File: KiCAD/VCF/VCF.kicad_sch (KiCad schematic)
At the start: 49 parts, among them J1 FM, J2 CV, J3 IN, J4 OUT, J5 Conn_01x03, J6 Conn_01x03, Q1 2N3904, SW1 SW_SPDT, SW2 SW_SPDT, U1 TL072, U2 TL072, U3 UA776, U4 UA776, U5 TL072

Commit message: Vertical Resistor Footprint
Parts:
- R1, R10, R11, R12, R13, R14, R15, R16, R17, R18, R19, R2, R20, R21, R22, R23, R24, R25, R26, R27, R3, R4, R5, R6, R7, R8, R9: footprint HackSynth:R_Axial_DIN0207_L6.3mm_D2.5mm_P7.62mm_Horizontal -> HackSynth:R_Vertical_P2.54mm
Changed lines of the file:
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@@
 			)
 		)
-		(property "Footprint" "HackSynth:R_Axial_DIN0207_L6.3mm_D2.5mm_P7.62mm_Horizontal"
+		(property "Footprint" "HackSynth:R_Vertical_P2.54mm"
 			(at 116.84 170.942 90)
 			(effects
@@
 			)
 		)
-		(property "Footprint" "HackSynth:R_Axial_DIN0207_L6.3mm_D2.5mm_P7.62mm_Horizontal"
+		(property "Footprint" "HackSynth:R_Vertical_P2.54mm"
 			(at 92.71 117.602 90)
 			(effects
@@
 			)
 		)
-		(property "Footprint" "HackSynth:R_Axial_DIN0207_L6.3mm_D2.5mm_P7.62mm_Horizontal"
+		(property "Footprint" "HackSynth:R_Vertical_P2.54mm"
 			(at 101.6 78.232 90)
 			(effects
@@
 			)
 		)
-		(property "Footprint" "HackSynth:R_Axial_DIN0207_L6.3mm_D2.5mm_P7.62mm_Horizontal"
+		(property "Footprint" "HackSynth:R_Vertical_P2.54mm"
 			(at 89.662 90.17 90)
 			(effects
@@
 			)
 		)
-		(property "Footprint" "HackSynth:R_Axial_DIN0207_L6.3mm_D2.5mm_P7.62mm_Horizontal"
+		(property "Footprint" "HackSynth:R_Vertical_P2.54mm"
 			(at 138.938 41.91 90)
 			(effects
@@
 			)
 		)
-		(property "Footprint" "HackSynth:R_Axial_DIN0207_L6.3mm_D2.5mm_P7.62mm_Horizontal"
+		(property "Footprint" "HackSynth:R_Vertical_P2.54mm"
 			(at 141.478 111.76 90)
 			(effects
@@
 			)
 		)
-		(property "Footprint" "HackSynth:R_Axial_DIN0207_L6.3mm_D2.5mm_P7.62mm_Horizontal"
+		(property "Footprint" "HackSynth:R_Vertical_P2.54mm"
 			(at 227.33 109.982 90)
 			(effects
@@
 			)
 		)
-		(property "Footprint" "HackSynth:R_Axial_DIN0207_L6.3mm_D2.5mm_P7.62mm_Horizontal"
+		(property "Footprint" "HackSynth:R_Vertical_P2.54mm"
 			(at 114.3 78.232 90)
 			(effects
@@
 			)
 		)
-		(property "Footprint" "HackSynth:R_Axial_DIN0207_L6.3mm_D2.5mm_P7.62mm_Horizontal"
+		(property "Footprint" "HackSynth:R_Vertical_P2.54mm"
 			(at 205.232 93.98 90)
 			(effects
@@
 			)
 		)
-		(property "Footprint" "HackSynth:R_Axial_DIN0207_L6.3mm_D2.5mm_P7.62mm_Horizontal"
+		(property "Footprint" "HackSynth:R_Vertical_P2.54mm"
 			(at 97.79 50.292 90)
 			(effects
@@
 			)
 		)
-		(property "Footprint" "HackSynth:R_Axial_DIN0207_L6.3mm_D2.5mm_P7.62mm_Horizontal"
+		(property "Footprint" "HackSynth:R_Vertical_P2.54mm"
 			(at 127.762 133.35 90)
 			(effects
@@
 			)
 		)
-		(property "Footprint" "HackSynth:R_Axial_DIN0207_L6.3mm_D2.5mm_P7.62mm_Horizontal"
+		(property "Footprint" "HackSynth:R_Vertical_P2.54mm"
 			(at 137.922 133.35 90)
 			(effects
@@
 			)
 		)
-		(property "Footprint" "HackSynth:R_Axial_DIN0207_L6.3mm_D2.5mm_P7.62mm_Horizontal"
+		(property "Footprint" "HackSynth:R_Vertical_P2.54mm"
 			(at 227.33 71.882 90)
 			(effects
@@
 			)
 		)
-		(property "Footprint" "HackSynth:R_Axial_DIN0207_L6.3mm_D2.5mm_P7.62mm_Horizontal"
+		(property "Footprint" "HackSynth:R_Vertical_P2.54mm"
 			(at 172.212 133.35 90)
 			(effects
@@
 			)
 		)
-		(property "Footprint" "HackSynth:R_Axial_DIN0207_L6.3mm_D2.5mm_P7.62mm_Horizontal"
+		(property "Footprint" "HackSynth:R_Vertical_P2.54mm"
 			(at 205.232 133.35 90)
 			(effects
@@
 			)
 		)
-		(property "Footprint" "HackSynth:R_Axial_DIN0207_L6.3mm_D2.5mm_P7.62mm_Horizontal"
+		(property "Footprint" "HackSynth:R_Vertical_P2.54mm"
 			(at 123.19 117.602 90)
 			(effects
@@
 			)
 		)
-		(property "Footprint" "HackSynth:R_Axial_DIN0207_L6.3mm_D2.5mm_P7.62mm_Horizontal"
+		(property "Footprint" "HackSynth:R_Vertical_P2.54mm"
 			(at 212.852 133.35 90)
 			(effects
@@
 			)
 		)
-		(property "Footprint" "HackSynth:R_Axial_DIN0207_L6.3mm_D2.5mm_P7.62mm_Horizontal"
+		(property "Footprint" "HackSynth:R_Vertical_P2.54mm"
 			(at 73.66 57.912 90)
 			(effects
@@
 			)
 		)
-		(property "Footprint" "HackSynth:R_Axial_DIN0207_L6.3mm_D2.5mm_P7.62mm_Horizontal"
+		(property "Footprint" "HackSynth:R_Vertical_P2.54mm"
 			(at 134.62 158.242 90)
 			(effects
@@
 			)
 		)
-		(property "Footprint" "HackSynth:R_Axial_DIN0207_L6.3mm_D2.5mm_P7.62mm_Horizontal"
+		(property "Footprint" "HackSynth:R_Vertical_P2.54mm"
 			(at 150.622 99.06 90)
 			(effects
@@
 			)
 		)
-		(property "Footprint" "HackSynth:R_Axial_DIN0207_L6.3mm_D2.5mm_P7.62mm_Horizontal"
+		(property "Footprint" "HackSynth:R_Vertical_P2.54mm"
 			(at 54.61 31.242 90)
 			(effects
@@
 			)
 		)
-		(property "Footprint" "HackSynth:R_Axial_DIN0207_L6.3mm_D2.5mm_P7.62mm_Horizontal"
+		(property "Footprint" "HackSynth:R_Vertical_P2.54mm"
 			(at 230.632 133.35 90)
 			(effects
@@
 			)
 		)
-		(property "Footprint" "HackSynth:R_Axial_DIN0207_L6.3mm_D2.5mm_P7.62mm_Horizontal"
+		(property "Footprint" "HackSynth:R_Vertical_P2.54mm"
 			(at 184.912 99.06 90)
 			(effects
@@
 			)
 		)
-		(property "Footprint" "HackSynth:R_Axial_DIN0207_L6.3mm_D2.5mm_P7.62mm_Horizontal"
+		(property "Footprint" "HackSynth:R_Vertical_P2.54mm"
 			(at 54.61 57.912 90)
 			(effects
@@
 			)
 		)
-		(property "Footprint" "HackSynth:R_Axial_DIN0207_L6.3mm_D2.5mm_P7.62mm_Horizontal"
+		(property "Footprint" "HackSynth:R_Vertical_P2.54mm"
 			(at 167.64 117.602 90)
 			(effects
@@
 			)
 		)
-		(property "Footprint" "HackSynth:R_Axial_DIN0207_L6.3mm_D2.5mm_P7.62mm_Horizontal"
+		(property "Footprint" "HackSynth:R_Vertical_P2.54mm"
 			(at 230.632 93.98 90)
 			(effects
@@
 			)
 		)
-		(property "Footprint" "HackSynth:R_Axial_DIN0207_L6.3mm_D2.5mm_P7.62mm_Horizontal"
+		(property "Footprint" "HackSynth:R_Vertical_P2.54mm"
 			(at 212.852 93.98 90)
 			(effects

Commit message: VCF PCB
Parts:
- removed RV1: 100k, HackSynth:Potentiometer_Alps_RK09K_Horizontal, symbol HackSynth:R_Potentiometer
- added RV1: R_Trim 100k, HackSynth:TrimPot_Bourns_3339S_Horizontal, symbol HackSynth:R_Potentiometer_Trim
- R1, R10, R11, R12, R13, R14, R15, R16, R17, R18, R19, R2, R20, R21, R22, R23, R24, R25, R26, R27, R3, R4, R5, R6, R7, R8, R9: footprint HackSynth:R_Vertical_P2.54mm -> HackSynth:R_Axial_DIN0207_L6.3mm_D2.5mm_P7.62mm_Horizontal
- renumbered SW1 to HARD/SOFT1, SW2 to LP/BP1
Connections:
- net at R5.2: now also RV1.1
- net at J2.T: now also RV1.2, RV1.3
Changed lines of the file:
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@@
 			)
 		)
-		(property "Footprint" "HackSynth:R_Vertical_P2.54mm"
+		(property "Footprint" "HackSynth:R_Axial_DIN0207_L6.3mm_D2.5mm_P7.62mm_Horizontal"
 			(at 116.84 170.942 90)
 			(effects
@@
 			)
 		)
-		(property "Footprint" "HackSynth:R_Vertical_P2.54mm"
+		(property "Footprint" "HackSynth:R_Axial_DIN0207_L6.3mm_D2.5mm_P7.62mm_Horizontal"
 			(at 92.71 117.602 90)
 			(effects
@@
 			)
 		)
-		(property "Footprint" "HackSynth:R_Vertical_P2.54mm"
+		(property "Footprint" "HackSynth:R_Axial_DIN0207_L6.3mm_D2.5mm_P7.62mm_Horizontal"
 			(at 101.6 78.232 90)
 			(effects
@@
 			)
 		)
-		(property "Footprint" "HackSynth:R_Vertical_P2.54mm"
+		(property "Footprint" "HackSynth:R_Axial_DIN0207_L6.3mm_D2.5mm_P7.62mm_Horizontal"
 			(at 89.662 90.17 90)
 			(effects
@@
 			)
 		)
-		(property "Footprint" "HackSynth:R_Vertical_P2.54mm"
+		(property "Footprint" "HackSynth:R_Axial_DIN0207_L6.3mm_D2.5mm_P7.62mm_Horizontal"
 			(at 138.938 41.91 90)
 			(effects
@@
 			)
 		)
-		(property "Footprint" "HackSynth:R_Vertical_P2.54mm"
+		(property "Footprint" "HackSynth:R_Axial_DIN0207_L6.3mm_D2.5mm_P7.62mm_Horizontal"
 			(at 141.478 111.76 90)
 			(effects
@@
 			)
 		)
-		(property "Footprint" "HackSynth:R_Vertical_P2.54mm"
+		(property "Footprint" "HackSynth:R_Axial_DIN0207_L6.3mm_D2.5mm_P7.62mm_Horizontal"
 			(at 227.33 109.982 90)
 			(effects
@@
 		(on_board yes)
 		(dnp no)
-		(property "Reference" "SW1"
+		(property "Reference" "HARD/SOFT1"
 			(at 156.21 151.384 0)
 			(effects
@@
 			(project "VCF"
 				(path "/33bfd214-aaee-4460-96d4-9e01d485922e"
-					(reference "SW1")
+					(reference "HARD/SOFT1")
 					(unit 1)
 				)
@@
 			)
 		)
-		(property "Footprint" "HackSynth:R_Vertical_P2.54mm"
+		(property "Footprint" "HackSynth:R_Axial_DIN0207_L6.3mm_D2.5mm_P7.62mm_Horizontal"
 			(at 114.3 78.232 90)
 			(effects
@@
 			)
 		)
-		(property "Footprint" "HackSynth:R_Vertical_P2.54mm"
+		(property "Footprint" "HackSynth:R_Axial_DIN0207_L6.3mm_D2.5mm_P7.62mm_Horizontal"
 			(at 205.232 93.98 90)
 			(effects
@@
 			)
 		)
-		(property "Footprint" "HackSynth:R_Vertical_P2.54mm"
+		(property "Footprint" "HackSynth:R_Axial_DIN0207_L6.3mm_D2.5mm_P7.62mm_Horizontal"
 			(at 97.79 50.292 90)
 			(effects
@@
 			)
 		)
-		(property "Footprint" "HackSynth:R_Vertical_P2.54mm"
+		(property "Footprint" "HackSynth:R_Axial_DIN0207_L6.3mm_D2.5mm_P7.62mm_Horizontal"
 			(at 127.762 133.35 90)
 			(effects
@@
 			)
 		)
-		(property "Footprint" "HackSynth:R_Vertical_P2.54mm"
+		(property "Footprint" "HackSynth:R_Axial_DIN0207_L6.3mm_D2.5mm_P7.62mm_Horizontal"
 			(at 137.922 133.35 90)
 			(effects
@@
 			)
 		)
-		(property "Footprint" "HackSynth:R_Vertical_P2.54mm"
+		(property "Footprint" "HackSynth:R_Axial_DIN0207_L6.3mm_D2.5mm_P7.62mm_Horizontal"
 			(at 227.33 71.882 90)
 			(effects
@@
 			)
 		)
-		(property "Footprint" "HackSynth:R_Vertical_P2.54mm"
+		(property "Footprint" "HackSynth:R_Axial_DIN0207_L6.3mm_D2.5mm_P7.62mm_Horizontal"
 			(at 172.212 133.35 90)
 			(effects
@@
 			)
 		)
-		(property "Footprint" "HackSynth:R_Vertical_P2.54mm"
+		(property "Footprint" "HackSynth:R_Axial_DIN0207_L6.3mm_D2.5mm_P7.62mm_Horizontal"
 			(at 205.232 133.35 90)
 			(effects
@@
 	)
 	(symbol
+		(lib_id "HackSynth:R_Potentiometer_Trim")
+		(at 82.55 119.38 270)
+		(unit 1)
+		(exclude_from_sim no)
+		(in_bom yes)
+		(on_board yes)
+		(dnp no)
+		(fields_autoplaced yes)
+		(property "Reference" "RV1"
+			(at 82.55 113.03 90)
+			(effects
+				(font
+					(size 1.27 1.27)
+				)
+			)
+		)
+		(property "Value" "R_Trim 100k"
+			(at 82.55 115.57 90)
+			(effects
+				(font
+					(size 1.27 1.27)
+				)
+			)
+		)
+		(property "Footprint" "HackSynth:TrimPot_Bourns_3339S_Horizontal"
+			(at 82.55 119.38 0)
+			(effects
+				(font
+					(size 1.27 1.27)
+				)
+				(hide yes)
+			)
+		)
+		(property "Datasheet" "~"
+			(at 82.55 119.38 0)
+			(effects
+				(font
+					(size 1.27 1.27)
+				)
+				(hide yes)
+			)
+		)
+		(property "Description" "Trim-potentiometer"
+			(at 82.55 119.38 0)
+			(effects
+				(font
+					(size 1.27 1.27)
+				)
+				(hide yes)
+			)
+		)
+		(pin "2"
+		)
+		(pin "1"
+		)
+		(pin "3"
+		)
+		(instances
+			(project ""
+				(path "/33bfd214-aaee-4460-96d4-9e01d485922e"
+					(reference "RV1")
+					(unit 1)
+				)
+			)
+		)
+	)
+	(symbol
 		(lib_id "HackSynth:R")
 		(at 123.19 119.38 270)
@@
 			)
 		)
-		(property "Footprint" "HackSynth:R_Vertical_P2.54mm"
+		(property "Footprint" "HackSynth:R_Axial_DIN0207_L6.3mm_D2.5mm_P7.62mm_Horizontal"
 			(at 123.19 117.602 90)
 			(effects
@@
 			)
 		)
-		(property "Footprint" "HackSynth:R_Vertical_P2.54mm"
+		(property "Footprint" "HackSynth:R_Axial_DIN0207_L6.3mm_D2.5mm_P7.62mm_Horizontal"
 			(at 212.852 133.35 90)
 			(effects
@@
 	)
 	(symbol
-		(lib_id "HackSynth:R_Potentiometer")
-		(at 82.55 119.38 270)
-		(unit 1)
-		(exclude_from_sim no)
-		(in_bom yes)
-		(on_board yes)
-		(dnp no)
-		(property "Reference" "RV1"
-			(at 82.55 113.03 90)
-			(effects
-				(font
-					(size 1.27 1.27)
-				)
-			)
-		)
-		(property "Value" "100k"
-			(at 82.55 115.57 90)
-			(effects
-				(font
-					(size 1.27 1.27)
-				)
-			)
-		)
-		(property "Footprint" "HackSynth:Potentiometer_Alps_RK09K_Horizontal"
-			(at 82.55 119.38 0)
-			(effects
-				(font
-					(size 1.27 1.27)
-				)
-				(hide yes)
-			)
-		)
-		(property "Datasheet" "~"
-			(at 82.55 119.38 0)
-			(effects
-				(font
-					(size 1.27 1.27)
-				)
-				(hide yes)
-			)
-		)
-		(property "Description" "Potentiometer"
-			(at 82.55 119.38 0)
-			(effects
-				(font
-					(size 1.27 1.27)
-				)
-				(hide yes)
-			)
-		)
-		(pin "2"
-		)
-		(pin "1"
-		)
-		(pin "3"
-		)
-		(instances
-			(project "VCF"
-				(path "/33bfd214-aaee-4460-96d4-9e01d485922e"
-					(reference "RV1")
-					(unit 1)
-				)
-			)
-		)
-	)
-	(symbol
 		(lib_id "power:VSS")
 		(at 91.44 96.52 180)
@@
 			)
 		)
-		(property "Footprint" "HackSynth:R_Vertical_P2.54mm"
+		(property "Footprint" "HackSynth:R_Axial_DIN0207_L6.3mm_D2.5mm_P7.62mm_Horizontal"
 			(at 73.66 57.912 90)
 			(effects
@@
 			)
 		)
-		(property "Footprint" "HackSynth:R_Vertical_P2.54mm"
+		(property "Footprint" "HackSynth:R_Axial_DIN0207_L6.3mm_D2.5mm_P7.62mm_Horizontal"
 			(at 134.62 158.242 90)
 			(effects
@@
 			)
 		)
-		(property "Footprint" "HackSynth:R_Vertical_P2.54mm"
+		(property "Footprint" "HackSynth:R_Axial_DIN0207_L6.3mm_D2.5mm_P7.62mm_Horizontal"
 			(at 150.622 99.06 90)
 			(effects
@@
 			)
 		)
-		(property "Footprint" "HackSynth:R_Vertical_P2.54mm"
+		(property "Footprint" "HackSynth:R_Axial_DIN0207_L6.3mm_D2.5mm_P7.62mm_Horizontal"
 			(at 54.61 31.242 90)
 			(effects
@@
 			)
 		)
-		(property "Footprint" "HackSynth:R_Vertical_P2.54mm"
+		(property "Footprint" "HackSynth:R_Axial_DIN0207_L6.3mm_D2.5mm_P7.62mm_Horizontal"
 			(at 230.632 133.35 90)
 			(effects
@@
 			)
 		)
-		(property "Footprint" "HackSynth:R_Vertical_P2.54mm"
+		(property "Footprint" "HackSynth:R_Axial_DIN0207_L6.3mm_D2.5mm_P7.62mm_Horizontal"
 			(at 184.912 99.06 90)
 			(effects
@@
 			)
 		)
-		(property "Footprint" "HackSynth:R_Vertical_P2.54mm"
+		(property "Footprint" "HackSynth:R_Axial_DIN0207_L6.3mm_D2.5mm_P7.62mm_Horizontal"
 			(at 54.61 57.912 90)
 			(effects
@@
 			)
 		)
-		(property "Footprint" "HackSynth:R_Vertical_P2.54mm"
+		(property "Footprint" "HackSynth:R_Axial_DIN0207_L6.3mm_D2.5mm_P7.62mm_Horizontal"
 			(at 167.64 117.602 90)
 			(effects
@@
 			)
 		)
-		(property "Footprint" "HackSynth:R_Vertical_P2.54mm"
+		(property "Footprint" "HackSynth:R_Axial_DIN0207_L6.3mm_D2.5mm_P7.62mm_Horizontal"
 			(at 230.632 93.98 90)
 			(effects
@@
 			)
 		)
-		(property "Footprint" "HackSynth:R_Vertical_P2.54mm"
+		(property "Footprint" "HackSynth:R_Axial_DIN0207_L6.3mm_D2.5mm_P7.62mm_Horizontal"
 			(at 212.852 93.98 90)
 			(effects
@@
 		(on_board yes)
 		(dnp no)
-		(property "Reference" "SW2"
+		(property "Reference" "LP/BP1"
 			(at 243.84 99.822 0)
 			(effects
@@
 			(project "VCF"
 				(path "/33bfd214-aaee-4460-96d4-9e01d485922e"
-					(reference "SW2")
+					(reference "LP/BP1")
 					(unit 1)
 				)

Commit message: Delay PCB
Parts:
- C2: value 1uF -> 1µF
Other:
- title: VCF -> HackSynth VCF
- moved on the sheet: J5, J6, R25

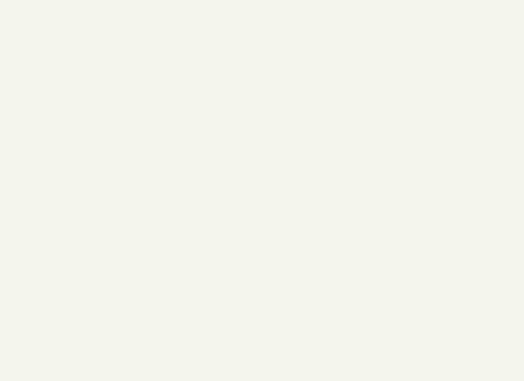
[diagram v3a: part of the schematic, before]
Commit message: Footprint Edits
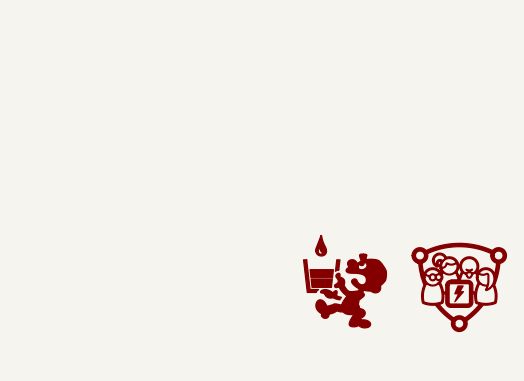
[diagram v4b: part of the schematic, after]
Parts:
- added G1: ~, symbol HackSynth:CCHS_Logo
- added G2: ~, symbol HackSynth:Logo_PancakeLegend
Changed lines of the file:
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@@
 	)
 	(symbol
+		(lib_id "HackSynth:CCHS_Logo")
+		(at 275.59 173.355 0)
+		(unit 1)
+		(exclude_from_sim no)
+		(in_bom yes)
+		(on_board yes)
+		(dnp no)
+		(fields_autoplaced yes)
+		(property "Reference" "G1"
+			(at 275.59 180.975 0)
+			(effects
+				(font
+					(size 1.27 1.27)
+				)
+				(hide yes)
+			)
+		)
+		(property "Value" "~"
+			(at 281.94 174.525 0)
+			(effects
+				(font
+					(size 1.27 1.27)
+				)
+				(justify left)
+			)
+		)
+		(property "Footprint" ""
+			(at 275.59 173.355 0)
+			(effects
+				(font
+					(size 1.27 1.27)
+				)
+				(hide yes)
+			)
+		)
+		(property "Datasheet" ""
+			(at 275.59 173.355 0)
+			(effects
+				(font
+					(size 1.27 1.27)
+				)
+				(hide yes)
+			)
+		)
+		(property "Description" ""
+			(at 275.59 173.355 0)
+			(effects
+				(font
+					(size 1.27 1.27)
+				)
+				(hide yes)
+			)
+		)
+		(instances
+			(project "VCF"
+				(path "/33bfd214-aaee-4460-96d4-9e01d485922e"
+					(reference "G1")
+					(unit 1)
+				)
+			)
+		)
+	)
+	(symbol
 		(lib_id "HackSynth:R")
 		(at 137.16 41.91 0)
@@
 				)
 			)
+		)
+	)
+	(symbol
+		(lib_id "HackSynth:Logo_PancakeLegend")
+		(at 262.89 173.99 0)
+		(unit 1)
+		(exclude_from_sim no)
+		(in_bom yes)
+		(on_board yes)
+		(dnp no)
+		(fields_autoplaced yes)
+		(property "Reference" "G2"
+			(at 262.89 181.61 0)
+			(effects
+				(font
+					(size 1.27 1.27)
+				)
+				(hide yes)
+			)
+		)
+		(property "Value" "~"
+			(at 269.24 173.8899 0)
+			(effects
+				(font
+					(size 1.27 1.27)
+				)
+				(justify left)
+			)
+		)
+		(property "Footprint" ""
+			(at 262.89 173.99 0)
+			(effects
+				(font
+					(size 1.27 1.27)
+				)
+				(hide yes)
+			)
+		)
+		(property "Datasheet" ""
+			(at 262.89 173.99 0)
+			(effects
+				(font
+					(size 1.27 1.27)
+				)
+				(hide yes)
+			)
+		)
+		(property "Description" ""
+			(at 262.89 173.99 0)
+			(effects
+				(font
+					(size 1.27 1.27)
+				)
+				(hide yes)
+			)
+		)
+		(instances
+			(project "VCF"
+				(path "/33bfd214-aaee-4460-96d4-9e01d485922e"
+					(reference "G2")
+					(unit 1)
+				)
+			)

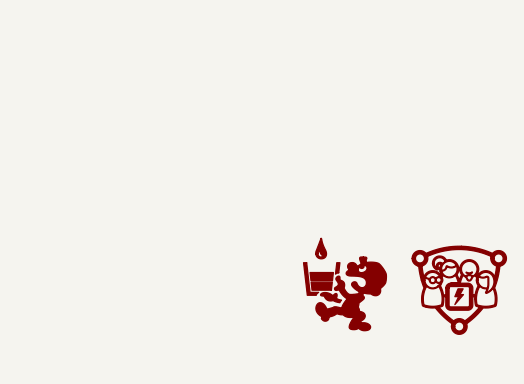
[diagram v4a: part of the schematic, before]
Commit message: Chorus PCB Dread + Footprint Edit
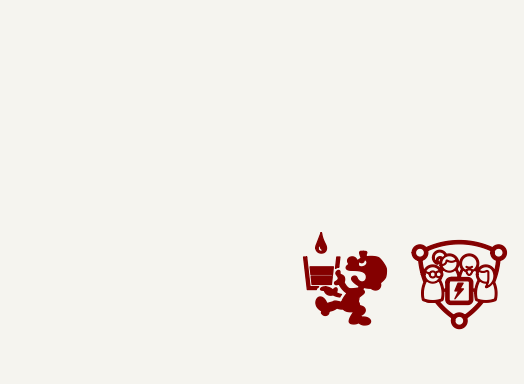
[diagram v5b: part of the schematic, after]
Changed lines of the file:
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@@
 	(symbol
 		(lib_id "HackSynth:CCHS_Logo")
-		(at 275.59 173.355 0)
+		(at 275.59 172.72 0)
 		(unit 1)
 		(exclude_from_sim no)
@@
 		(fields_autoplaced yes)
 		(property "Reference" "G1"
-			(at 275.59 180.975 0)
+			(at 275.59 180.34 0)
 			(effects
 				(font
@@
 		)
 		(property "Value" "~"
-			(at 281.94 174.525 0)
+			(at 281.94 173.89 0)
 			(effects
 				(font
@@
 		)
 		(property "Footprint" ""
-			(at 275.59 173.355 0)
+			(at 275.59 172.72 0)
 			(effects
 				(font
@@
 		)
 		(property "Datasheet" ""
-			(at 275.59 173.355 0)
+			(at 275.59 172.72 0)
 			(effects
 				(font
@@
 		)
 		(property "Description" ""
-			(at 275.59 173.355 0)
+			(at 275.59 172.72 0)
 			(effects
 				(font
@@
 	(symbol
 		(lib_id "HackSynth:Logo_PancakeLegend")
-		(at 262.89 173.99 0)
+		(at 262.89 173.355 0)
 		(unit 1)
 		(exclude_from_sim no)
@@
 		(fields_autoplaced yes)
 		(property "Reference" "G2"
-			(at 262.89 181.61 0)
+			(at 262.89 180.975 0)
 			(effects
 				(font
@@
 		)
 		(property "Value" "~"
-			(at 269.24 173.8899 0)
+			(at 269.24 173.2549 0)
 			(effects
 				(font
@@
 		)
 		(property "Footprint" ""
-			(at 262.89 173.99 0)
+			(at 262.89 173.355 0)
 			(effects
 				(font
@@
 		)
 		(property "Datasheet" ""
-			(at 262.89 173.99 0)
+			(at 262.89 173.355 0)
 			(effects
 				(font
@@
 		)
 		(property "Description" ""
-			(at 262.89 173.99 0)
+			(at 262.89 173.355 0)
 			(effects
 				(font
